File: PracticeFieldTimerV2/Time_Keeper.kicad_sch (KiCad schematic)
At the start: 3 parts, among them U4 DS3231MZ_TRL

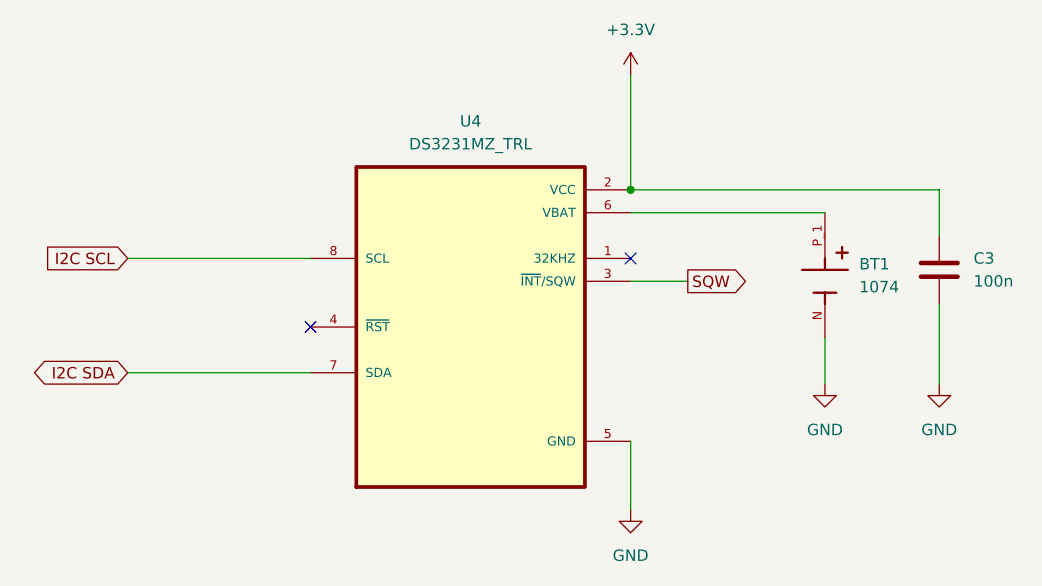
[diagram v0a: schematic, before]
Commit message: Add 10K pullup to SQW per DS3231 datasheet. Silly me!
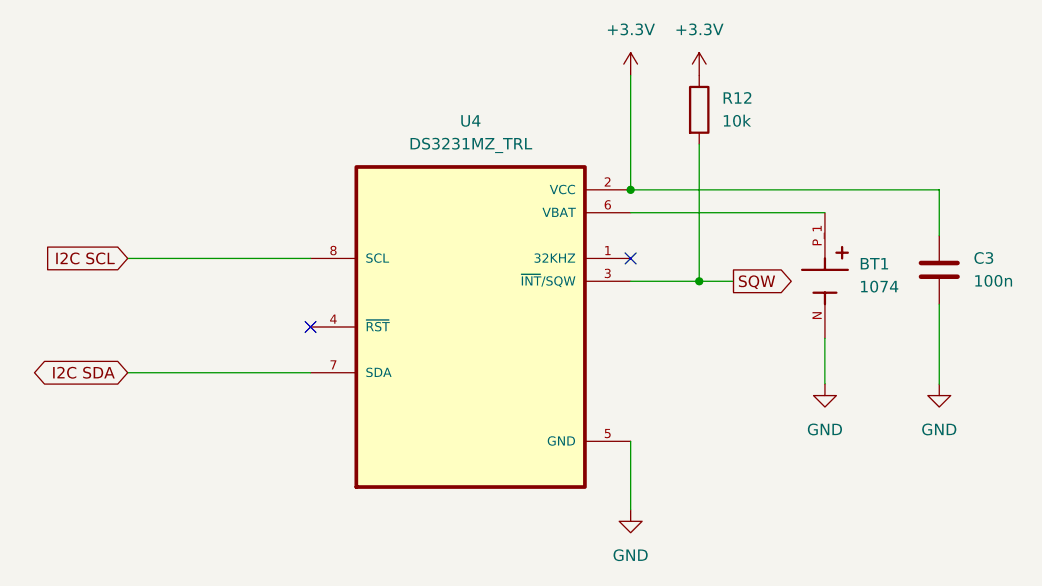
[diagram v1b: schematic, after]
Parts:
- added R12: 10k, Resistor_THT:R_Axial_DIN0207_L6.3mm_D2.5mm_P15.24mm_Horizontal, symbol Device:R
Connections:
- net +3.3V: now also R12.1
- net SQW: now also R12.2
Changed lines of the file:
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@@
+		(color 0 0 0 0)
+	)
+	(junction
+		(at 152.4 78.74)
+		(diameter 0)
 		(color 0 0 0 0)
 	)
@@
 	(wire
 		(pts
+			(xy 144.78 71.12) (xy 166.37 71.12)
+		)
+		(stroke
+			(width 0)
+			(type default)
+		)
+	)
+	(wire
+		(pts
 			(xy 166.37 85.09) (xy 166.37 90.17)
 		)
@@
 	(wire
 		(pts
-			(xy 144.78 78.74) (xy 151.13 78.74)
-		)
-		(stroke
-			(width 0)
-			(type default)
-		)
-	)
-	(wire
-		(pts
-			(xy 144.78 71.12) (xy 166.37 71.12)
+			(xy 152.4 63.5) (xy 152.4 78.74)
+		)
+		(stroke
+			(width 0)
+			(type default)
+		)
+	)
+	(wire
+		(pts
+			(xy 144.78 78.74) (xy 152.4 78.74)
+		)
+		(stroke
+			(width 0)
+			(type default)
+		)
+	)
+	(wire
+		(pts
+			(xy 152.4 78.74) (xy 156.21 78.74)
 		)
 		(stroke
@@
 	(global_label "SQW"
 		(shape output)
-		(at 151.13 78.74 0)
+		(at 156.21 78.74 0)
 		(fields_autoplaced yes)
 		(effects
@@
 		)
 		(property "Intersheetrefs" "${INTERSHEET_REFS}"
-			(at 158.1066 78.74 0)
+			(at 163.1866 78.74 0)
 			(effects
 				(font
@@
 	)
 	(symbol
+		(lib_id "Device:R")
+		(at 152.4 59.69 0)
+		(unit 1)
+		(exclude_from_sim no)
+		(in_bom yes)
+		(on_board yes)
+		(dnp no)
+		(fields_autoplaced yes)
+		(property "Reference" "R12"
+			(at 154.94 58.4199 0)
+			(effects
+				(font
+					(size 1.27 1.27)
+				)
+				(justify left)
+			)
+		)
+		(property "Value" "10k"
+			(at 154.94 60.9599 0)
+			(effects
+				(font
+					(size 1.27 1.27)
+				)
+				(justify left)
+			)
+		)
+		(property "Footprint" "Resistor_THT:R_Axial_DIN0207_L6.3mm_D2.5mm_P15.24mm_Horizontal"
+			(at 150.622 59.69 90)
+			(effects
+				(font
+					(size 1.27 1.27)
+				)
+				(hide yes)
+			)
+		)
+		(property "Datasheet" "~"
+			(at 152.4 59.69 0)
+			(effects
+				(font
+					(size 1.27 1.27)
+				)
+				(hide yes)
+			)
+		)
+		(property "Description" "Resistor"
+			(at 152.4 59.69 0)
+			(effects
+				(font
+					(size 1.27 1.27)
+				)
+				(hide yes)
+			)
+		)
+		(pin "2"
+		)
+		(pin "1"
+		)
+		(instances
+			(project ""
+				(path "/a82ebad5-0442-461b-8944-6652da9a0796/11c98f2b-89f7-4add-8042-04d6293d5f07"
+					(reference "R12")
+					(unit 1)
+				)
+			)
+		)
+	)
+	(symbol
 		(lib_id "power:+3.3V")
 		(at 144.78 55.88 0)
@@
 					(unit 1)
 				)
+			)
+		)
+	)
+	(symbol
+		(lib_id "power:+3.3V")
+		(at 152.4 55.88 0)
+		(unit 1)
+		(exclude_from_sim no)
+		(in_bom yes)
+		(on_board yes)
+		(dnp no)
+		(fields_autoplaced yes)
+		(property "Reference" "#PWR012"
+			(at 152.4 59.69 0)
+			(effects
+				(font
+					(size 1.27 1.27)
+				)
+				(hide yes)
+			)
+		)
+		(property "Value" "+3.3V"
+			(at 152.4 50.8 0)
+			(effects
+				(font
+					(size 1.27 1.27)
+				)
+			)
+		)
+		(property "Footprint" ""
+			(at 152.4 55.88 0)
+			(effects
+				(font
+					(size 1.27 1.27)
+				)
+				(hide yes)
+			)
+		)
+		(property "Datasheet" ""
+			(at 152.4 55.88 0)
+			(effects
+				(font
+					(size 1.27 1.27)
+				)
+				(hide yes)
+			)
+		)
+		(property "Description" "Power symbol creates a global label with name \"+3.3V\""
+			(at 152.4 55.88 0)
+			(effects
+				(font
+					(size 1.27 1.27)
+				)
+				(hide yes)
+			)
+		)
+		(pin "1"
+		)
+		(instances
+			(project "PracticeFieldTimerV2"
+				(path "/a82ebad5-0442-461b-8944-6652da9a0796/11c98f2b-89f7-4add-8042-04d6293d5f07"
+					(reference "#PWR012")
+					(unit 1)
+				)
